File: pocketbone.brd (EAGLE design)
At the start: 55 x 35 mm, 60 parts, among them J1 USD_CONNECTOR, U1 24LC_32AT-I/OT, U2 OSD3358, U3 SN74LVC1G07_DCK_5, Y1 CM200C-32.768KAZF-UT, Y2 445C33D24M00000

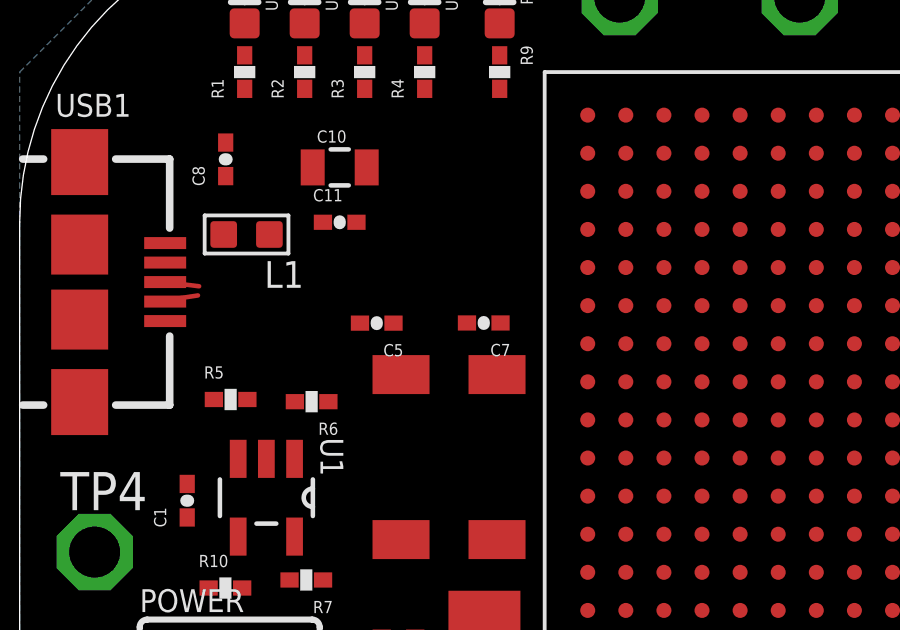
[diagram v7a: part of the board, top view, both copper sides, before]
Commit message: Routed USB1 DP/DN
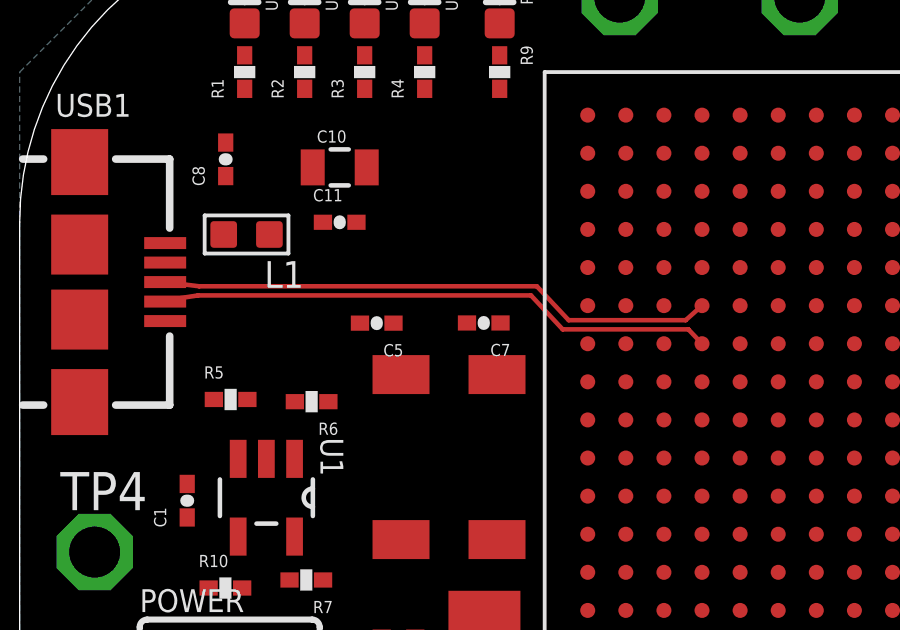
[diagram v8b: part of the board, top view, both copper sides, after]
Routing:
- net USB1_ID: track 1.12 -> 18.6 mm
- net USB1_DP: track 1.14 -> 18.6 mm
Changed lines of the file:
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@@
 <setting verticaltext="up"/>
 </settings>
-<grid distance="0.1" unitdist="mm" unit="mm" style="lines" multiple="1" display="no" altdistance="0.025" altunitdist="inch" altunit="inch"/>
+<grid distance="0.05" unitdist="mm" unit="mm" style="lines" multiple="1" display="no" altdistance="0.025" altunitdist="inch" altunit="inch"/>
 <layers>
 <layer number="1" name="Top" color="4" fill="1" visible="yes" active="yes"/>
@@
 <wire x1="9.1732" y1="19.013740625" x2="18.935" y2="24.755" width="0" layer="19" extent="1-1"/>
 <wire x1="7.5908" y1="19.086259375" x2="9.1732" y2="19.013740625" width="0" layer="19" extent="1-1"/>
-<wire x1="7.2836" y1="14.5164" x2="7.5908" y2="19.086259375" width="0" layer="19" extent="1-1"/>
+<wire x1="5.5852" y1="15.1536" x2="7.5908" y2="19.086259375" width="0" layer="19" extent="1-1"/>
+<wire x1="7.2836" y1="14.5164" x2="5.5852" y2="15.1536" width="0" layer="19" extent="1-1"/>
 <wire x1="7.4168" y1="12.8016" x2="7.2836" y2="14.5164" width="0" layer="19" extent="1-1"/>
 <wire x1="8.9954" y1="13.070140625" x2="7.4168" y2="12.8016" width="0" layer="19" extent="1-1"/>
-<wire x1="5.5852" y1="15.1536" x2="7.2836" y2="14.5164" width="0" layer="19" extent="1-1"/>
 <wire x1="6.8672" y1="26.5328" x2="7.5908" y2="19.086259375" width="0" layer="19" extent="1-1"/>
 </signal>
@@
 <contactref element="USB1" pad="D+"/>
 <wire x1="5.9828" y1="22.86" x2="4.85" y2="23" width="0.1524" layer="1"/>
-<wire x1="5.9828" y1="22.86" x2="22.745" y2="22.215" width="0" layer="19" extent="1-1"/>
+<wire x1="5.9828" y1="22.86" x2="17.24" y2="22.86" width="0.1524" layer="1"/>
+<wire x1="17.24" y1="22.86" x2="18.3" y2="21.729" width="0.1524" layer="1"/>
+<wire x1="18.3" y1="21.729" x2="22.2" y2="21.729" width="0.1524" layer="1"/>
+<wire x1="22.2" y1="21.729" x2="22.745" y2="22.215" width="0.1524" layer="1"/>
 </signal>
 <signal name="USB1_DM" class="2">
@@
 <wire x1="4.953" y1="22.4028" x2="4.9564" y2="22.4028" width="0.1524" layer="1"/>
 <wire x1="4.9564" y1="22.4028" x2="4.85" y2="22.35" width="0.1524" layer="1"/>
-<wire x1="5.9436" y1="22.5552" x2="22.745" y2="20.945" width="0" layer="19" extent="1-1"/>
+<wire x1="5.9436" y1="22.5552" x2="17.0448" y2="22.5552" width="0.1524" layer="1"/>
+<wire x1="17.0448" y1="22.5552" x2="18.1" y2="21.4238" width="0.1524" layer="1"/>
+<wire x1="18.1" y1="21.4238" x2="22.29" y2="21.4238" width="0.1524" layer="1"/>
+<wire x1="22.29" y1="21.4238" x2="22.745" y2="20.945" width="0.1524" layer="1"/>
 </signal>
 <signal name="N$1">
